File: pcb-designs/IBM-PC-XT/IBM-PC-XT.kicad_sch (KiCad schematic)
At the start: 9 parts, among them U1 8284A, U2 8088, U3 LS373, U4 LS244, U5 LS373, U6 LS245, U7 8087, U8 8259A, U9 8288

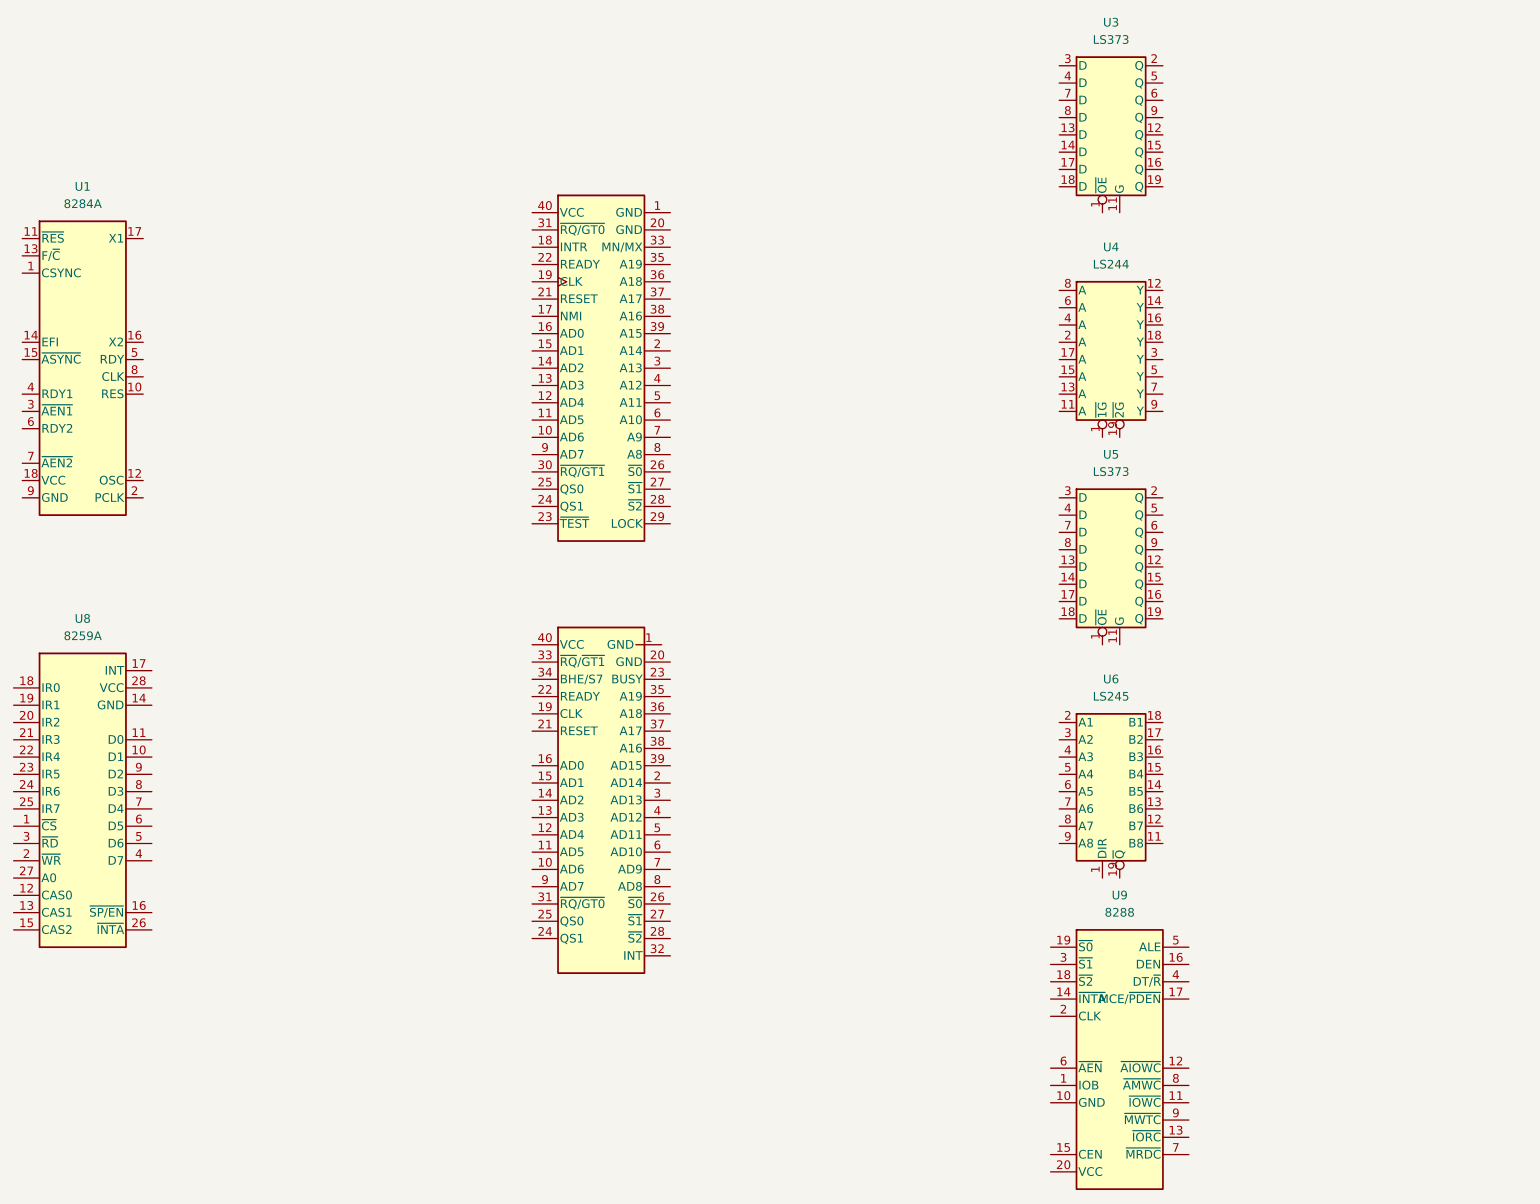
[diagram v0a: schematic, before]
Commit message: Added sheets as subpages
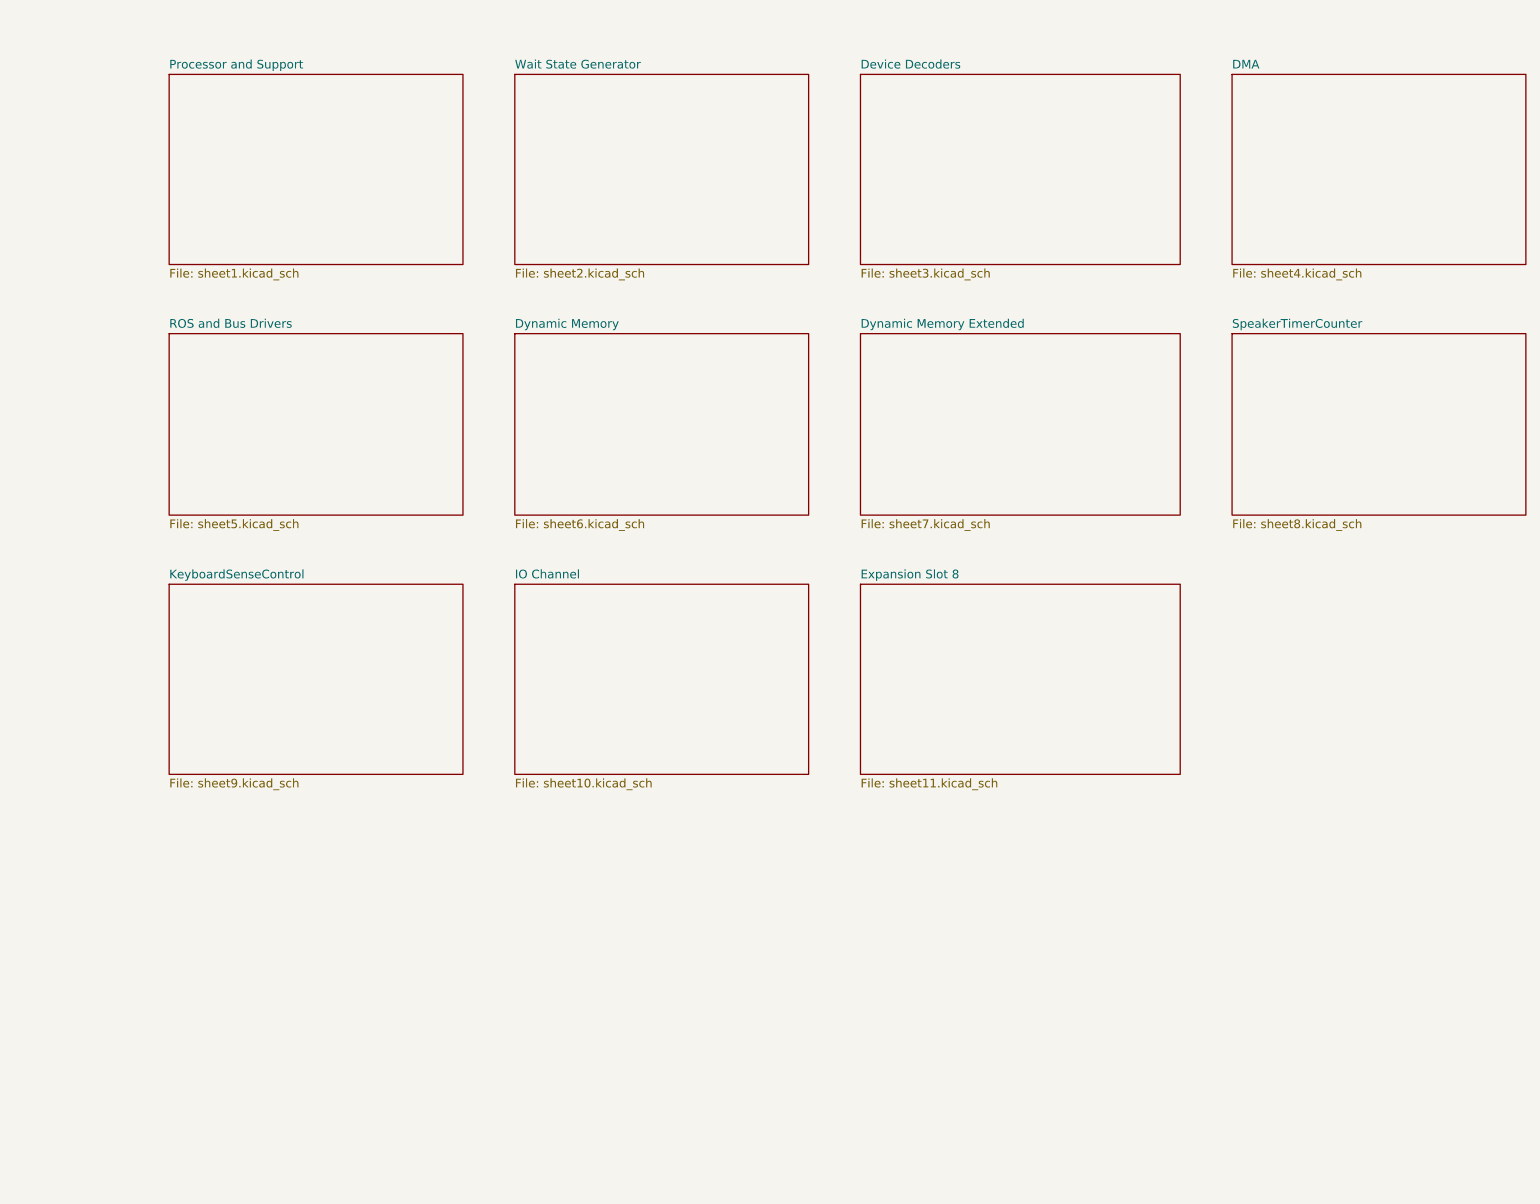
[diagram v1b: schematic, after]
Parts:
- removed U1: 8284A, Package_DIP:DIP-18_W7.62mm, symbol ibm_intel:8284A
- removed U2: 8088, Package_DIP:DIP-40_W15.24mm, symbol ibm_intel:8088
- removed U3, U5: LS373, symbol ibm_74xx:LS373
- removed U4: LS244, symbol ibm_74xx:LS244
- removed U6: LS245, symbol ibm_74xx:LS245
- removed U7: 8087, Package_DIP:DIP-40_W15.24mm, symbol ibm_intel:8087
- removed U8: 8259A, Package_DIP:DIP-28_W15.24mm, symbol ibm_intel:8259A
- removed U9: 8288, Package_DIP:DIP-20_W7.62mm, symbol ibm_intel:8288
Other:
- added sheet DMA (sheet4.kicad_sch)
- added sheet Device Decoders (sheet3.kicad_sch)
- added sheet Dynamic Memory (sheet6.kicad_sch)
- added sheet Dynamic Memory Extended (sheet7.kicad_sch)
- added sheet Expansion Slot 8 (sheet11.kicad_sch)
- added sheet IO Channel (sheet10.kicad_sch)
- added sheet KeyboardSenseControl (sheet9.kicad_sch)
- added sheet Processor and Support (sheet1.kicad_sch)
- added sheet ROS and Bus Drivers (sheet5.kicad_sch)
- added sheet SpeakerTimerCounter (sheet8.kicad_sch)
- added sheet Wait State Generator (sheet2.kicad_sch)
